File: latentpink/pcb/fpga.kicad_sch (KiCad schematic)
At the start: 36 parts, among them J9 XILINX_JTAG, M2 960-23-23-F-AB-0, U2 XC7K160T-2FBG484C

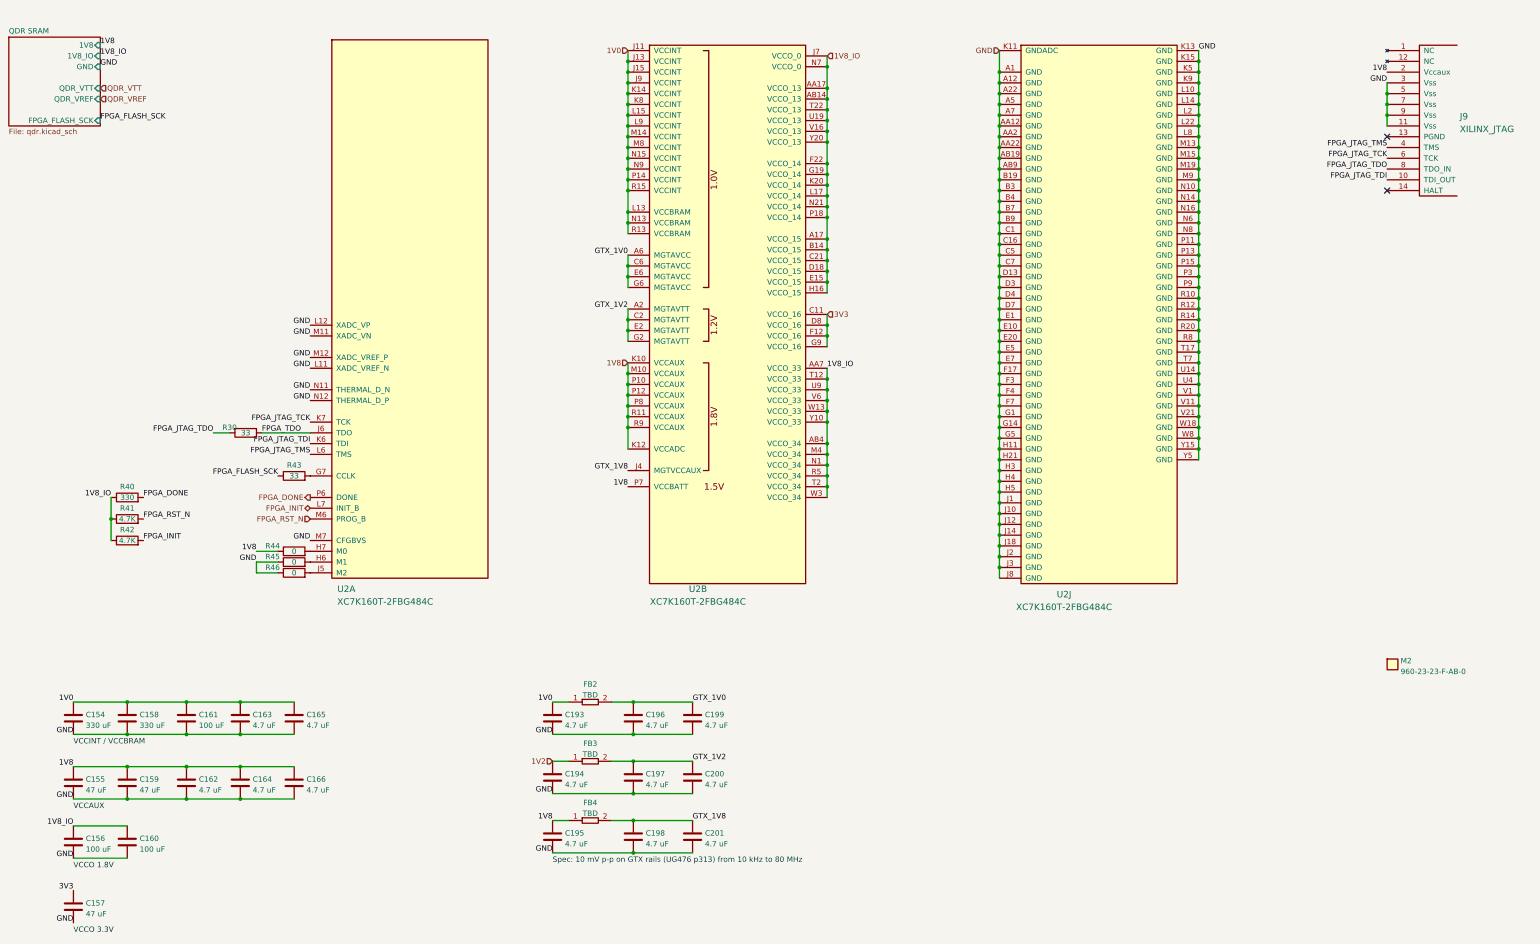
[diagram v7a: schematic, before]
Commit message: Continued footprint assignment and miscellaneous missing tidbits of schematic
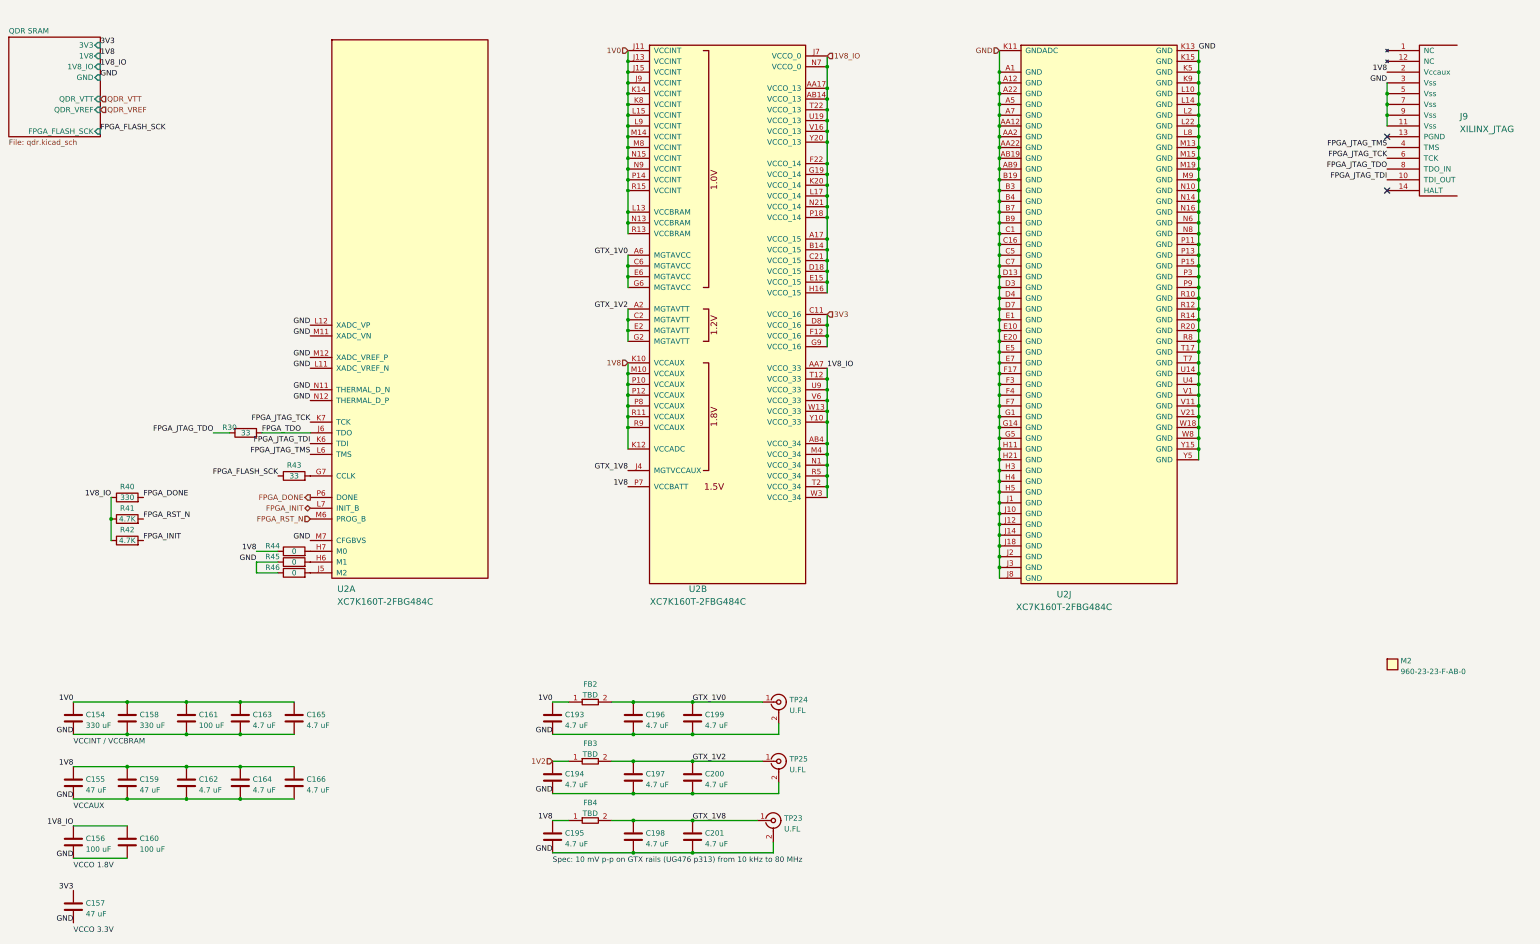
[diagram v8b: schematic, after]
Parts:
- added TP23, TP24, TP25: U.FL, azonenberg_pcb:CONN_U.FL_TE_1909763-1, symbol conn:CONN_COAXIAL
- C154, C155, C157, C158, C159: footprint (none) -> azonenberg_pcb:EIA_1210_CAP_NOSILK
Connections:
- net GND: now also TP23.2 (Ext), TP24.2 (Ext), TP25.2 (Ext)
- net GTX_1V0: now also TP24.1 (In)
- net GTX_1V2: now also TP25.1 (In)
- net GTX_1V8: now also TP23.1 (In)
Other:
- sheet QDR SRAM ports: added 3V3; removed none
